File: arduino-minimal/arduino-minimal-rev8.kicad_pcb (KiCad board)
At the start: 2 copper layers, 38 x 32 mm, 7 parts, among them J1 Conn_01x03, J2 Conn_01x02, U1 ATmega328P-AU

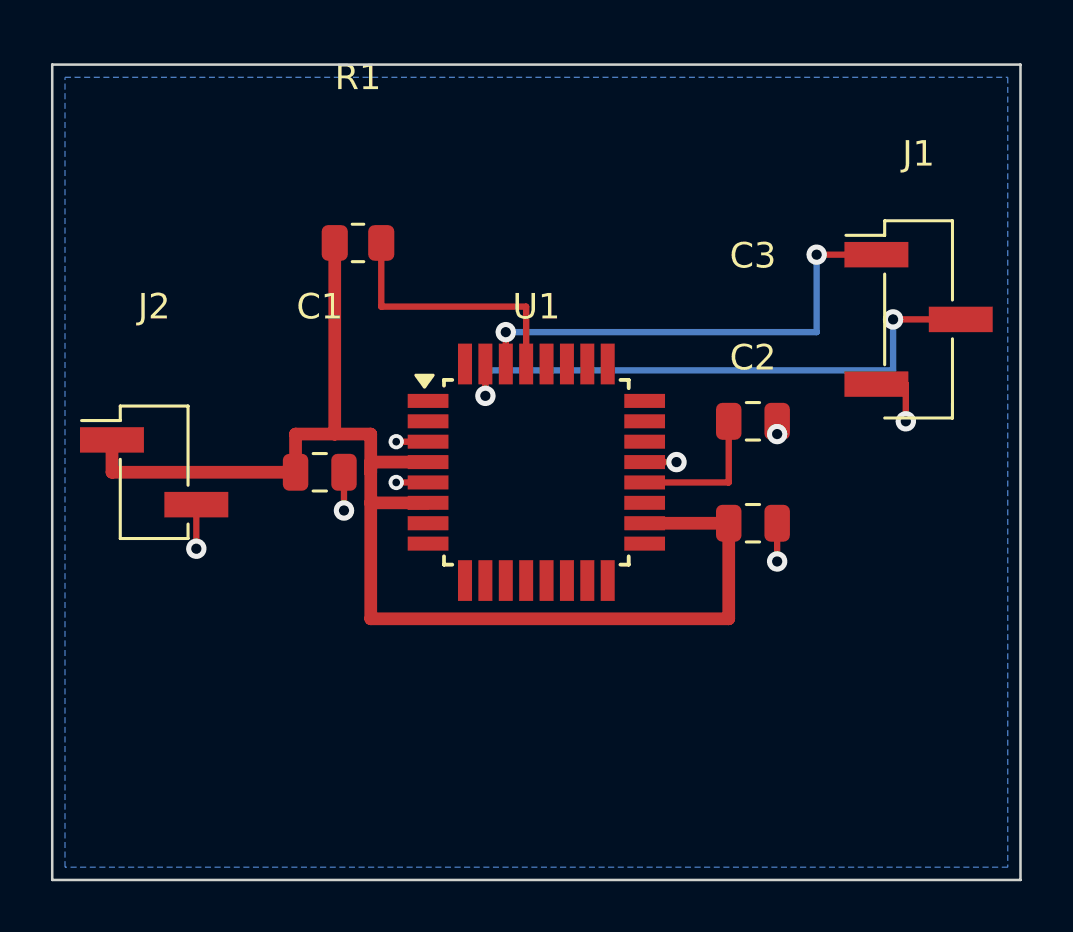
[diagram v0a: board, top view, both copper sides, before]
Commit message: arduino-minimal: rev8 PCB 45-degree routing rework (IPC-2221/JLC rules, zero 90-degree bends)
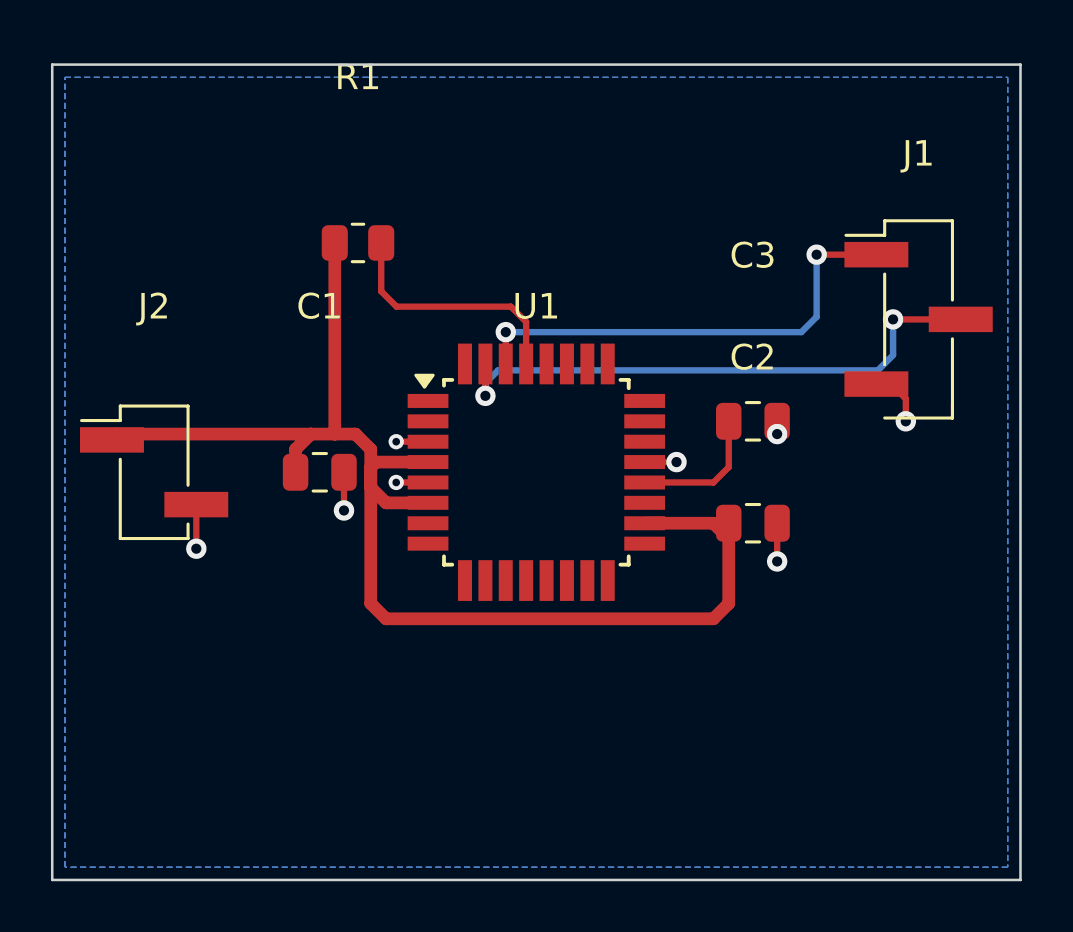
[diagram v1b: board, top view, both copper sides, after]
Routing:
- net VCC: track 53.7 -> 52.1 mm
- net Net-(U1-~{RESET}/PC6): track 10.4 -> 9.74 mm
- net /TX: track 22.9 -> 22.3 mm
